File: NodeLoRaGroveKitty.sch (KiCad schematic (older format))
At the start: 43 parts, among them IC1 CP2104, P1 PICKIT PROGRAMMER, P2 Battery, P3 A0, P4 D9, P5 USB_B, P6 I2C, Q1 Q_NPN_CBE, Q2 Q_NPN_CBE, SW2 SW_RESET, U1 AP2114, U2 MCP73831T-2ATI/OT, U3 ESP8266-12E

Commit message: Update BOM
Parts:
- C3: manf# (none) -> GRM21BR61A106KE19L
- IC1: maf# (none) -> CP2104-F03-GM
- P5: manf# (none) -> 105017-0001
- Q1, Q2: value Q_NPN_CBE -> MMBT2222A; manf# (none) -> MMBT2222A
- R16, R17: manf# (none) -> AF0805FR-0710KL
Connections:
- no-connect marks 41 -> 40
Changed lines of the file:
@@
 F 2 "" V 4270 5725 50  0000 C CNN
 F 3 "" V 4270 5725 50  0000 C CNN
+F 4 "105017-0001" H 4320 5825 60  0001 C CNN "manf#"
 	1    4320 5825
 	0    -1   -1   0
@@
 F 7 "USB to UART Bridge" H 5775 6220 50  0001 L CNN "Description"
 F 8 "None" H 5775 6220 50  0001 L CNN "Package"
+F 9 "CP2104-F03-GM" H 5775 6220 60  0001 C CNN "maf#"
 	1    5775 6220
 	1    0    0    -1
@@
 F 2 "" H 4905 6395 50  0000 C CNN
 F 3 "" H 4905 6395 50  0000 C CNN
+F 4 "GRM21BR61A106KE19L" H 4905 6395 60  0001 C CNN "manf#"
 	1    4905 6395
 	1    0    0    -1
@@
 P 5615 3255
 F 0 "Q2" H 5815 3305 50  0000 L CNN
-F 1 "Q_NPN_CBE" H 5815 3205 50  0000 L CNN
+F 1 "MMBT2222A" H 5815 3205 50  0000 L CNN
 F 2 "" H 5815 3355 50  0000 C CNN
 F 3 "" H 5615 3255 50  0000 C CNN
+F 4 "MMBT2222A" H 5615 3255 60  0001 C CNN "manf#"
 	1    5615 3255
 	1    0    0    1
@@
 F 2 "" H 5190 3255 50  0000 C CNN
 F 3 "" H 5190 3255 50  0000 C CNN
+F 4 "AF0805FR-0710KL" H 5190 3255 60  0001 C CNN "manf#"
 	1    5190 3255
 	0    1    1    0
@@
 P 5600 2630
 F 0 "Q1" H 5800 2680 50  0000 L CNN
-F 1 "Q_NPN_CBE" H 5800 2580 50  0000 L CNN
+F 1 "MMBT2222A" H 5800 2580 50  0000 L CNN
 F 2 "" H 5800 2730 50  0000 C CNN
 F 3 "" H 5600 2630 50  0000 C CNN
+F 4 "MMBT2222A" H 5600 2630 60  0001 C CNN "manf#"
 	1    5600 2630
 	1    0    0    -1
@@
 F 2 "" H 5175 2630 50  0000 C CNN
 F 3 "" H 5175 2630 50  0000 C CNN
+F 4 "AF0805FR-0710KL" H 5175 2630 60  0001 C CNN "manf#"
 	1    5175 2630
 	0    1    1    0
@@
 USB TO SERIAL CONVERTER
 NoConn ~ 4220 5525
-NoConn ~ 2215 2965
 $EndSCHEMATC

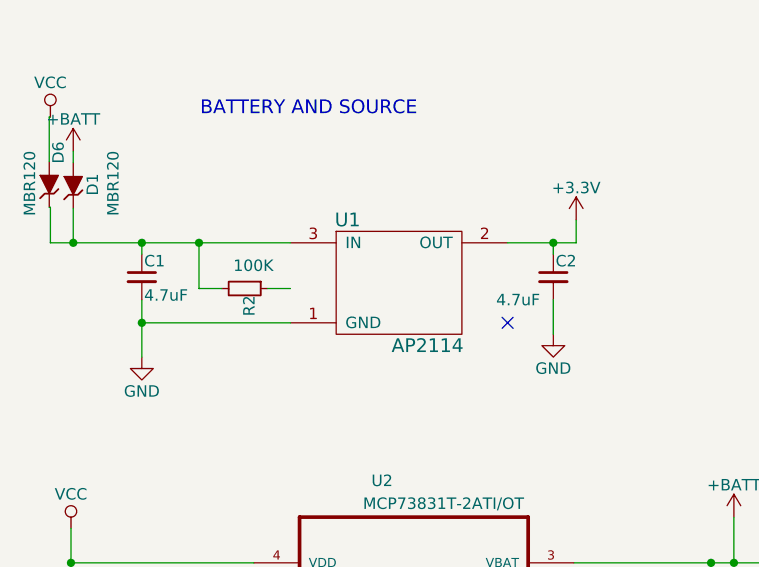
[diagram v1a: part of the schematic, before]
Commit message: Update AP2114, fix bugs JST
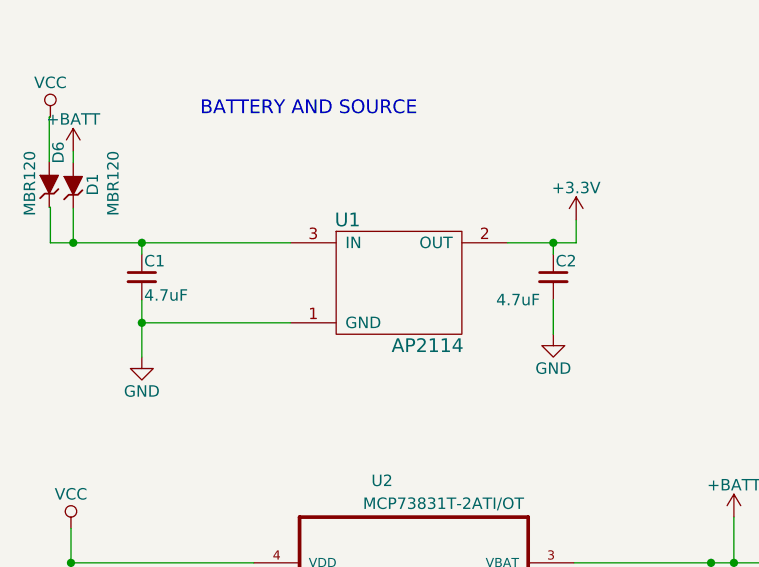
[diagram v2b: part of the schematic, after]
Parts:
- removed R2: 100K, Resistors_SMD:R_0805_HandSoldering, symbol R_Small
- A1: footprint TIH:GSG-SMA-EDGE -> Library:SMA_Conn_Ant
- C3: footprint (none) -> Capacitors_SMD:C_0805_HandSoldering
- D1, D6: footprint Diodes_SMD:SOD-123 -> Diodes_SMD:D_SOD-123
- IC1: footprint QFN24-PAD -> Housings_DFN_QFN:QFN-24_4x4mm_Pitch0.5mm_NoMask
- MODULE1: footprint TIH:RN2483 -> Library:RN2483
- P1: footprint Pin_Headers:Pin_Header_Straight_1x05 -> Pin_Headers:Pin_Header_Straight_1x05_Pitch2.54mm
- P2: footprint Pin_Headers:Pin_Header_Straight_1x02 -> Pin_Headers:Pin_Header_Angled_1x02_Pitch2.54mm
- P3, P4, P6: footprint Connectors_JST:JST_PH_S4B-PH-K_04x2.00mm_Angled -> Connectors_JST:JST_PH_S4B-PH-SM4-TB_04x2.00mm_Angled
- P5: footprint (none) -> LoraCat:MOLEX_105017-0001
- Q1, Q2: footprint (none) -> TO_SOT_Packages_SMD:SOT-23
- R16, R17: footprint (none) -> Resistors_SMD:R_0805_HandSoldering
- SW2: footprint TIH:SW_B3U-1000P -> Buttons_Switches_SMD:SW_SPST_B3U-1000P
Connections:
- no-connect marks 40 -> 39
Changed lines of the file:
@@
 LIBS:contrib
 LIBS:valves
-LIBS:theinventorhouse
 LIBS:USB6B1
 LIBS:MCP73831T-2ATI_OT
-LIBS:antena_good
 LIBS:RN2903-I_RM095
-LIBS:ESP32-footprints-Shem-Lib
 LIBS:CP2104
 LIBS:NodeLoRaGroveKitty-cache
+LIBS:ESP8266
 EELAYER 25 0
 EELAYER END
@@
 F 0 "MODULE1" H 1650 3550 50  0000 L CNN
 F 1 "RN2903" H 1650 750 50  0000 L CNN
-F 2 "TIH:RN2483" H 2250 2150 50  0001 L CNN
+F 2 "Library:RN2483" H 2250 2150 50  0001 L CNN
 F 3 "None" H 2250 2150 50  0001 L CNN
 F 4 "Sub-GHz Dual Band Long Range Transceiver LoRa Module" H 2250 2150 50  0001 L CNN "Description"
@@
 F 0 "P6" H 10950 5500 50  0000 C CNN
 F 1 "I2C" V 11050 5250 50  0000 C CNN
-F 2 "Connectors_JST:JST_PH_S4B-PH-K_04x2.00mm_Angled" H 10950 5250 50  0001 C CNN
+F 2 "Connectors_JST:JST_PH_S4B-PH-SM4-TB_04x2.00mm_Angled" H 10950 5250 50  0001 C CNN
 F 3 "" H 10950 5250 50  0000 C CNN
 F 4 "110990037" H 10950 5250 60  0001 C CNN "manf#"
 	1    10950 5250
 	1    0    0    -1
-$EndComp
-$Comp
-L R_Small R2
-U 1 1 57D1B196
-P 1445 5605
-F 0 "R2" H 1475 5625 50  0000 L CNN
-F 1 "100K" V 1345 5555 50  0000 L CNN
-F 2 "Resistors_SMD:R_0805_HandSoldering" H 1445 5605 50  0001 C CNN
-F 3 "" H 1445 5605 50  0000 C CNN
-F 4 "WR08X1003FTL" H 1445 5605 60  0001 C CNN "manf#"
-	1    1445 5605
-	0    1    1    0
 $EndComp
 $Comp
@@
 F 0 "D1" H 700 5070 50  0000 C CNN
 F 1 "MBR120" H 705 4980 50  0000 C CNN
-F 2 "Diodes_SMD:SOD-123" H 695 5155 50  0001 C CNN
+F 2 "Diodes_SMD:D_SOD-123" H 695 5155 50  0001 C CNN
 F 3 "" H 695 5155 50  0000 C CNN
 F 4 "NRVB120VLSFT1G" H 695 5155 60  0001 C CNN "manf#"
@@
 	0    -1   -1   0
 $EndComp
-NoConn ~ 2595 5755
 $Comp
 L +3.3V #PWR04
@@
 F 0 "P2" H 3935 7005 50  0000 C CNN
 F 1 "Battery" V 4035 6855 50  0000 C CNN
-F 2 "Pin_Headers:Pin_Header_Straight_1x02" H 3935 6855 50  0001 C CNN
+F 2 "Pin_Headers:Pin_Header_Angled_1x02_Pitch2.54mm" H 3935 6855 50  0001 C CNN
 F 3 "" H 3935 6855 50  0000 C CNN
 	1    3935 6855
@@
 F 0 "SW2" H 8630 3770 50  0000 C CNN
 F 1 "SW_RESET" H 8480 3580 50  0000 C CNN
-F 2 "TIH:SW_B3U-1000P" H 8480 3660 50  0001 C CNN
+F 2 "Buttons_Switches_SMD:SW_SPST_B3U-1000P" H 8480 3660 50  0001 C CNN
 F 3 "" H 8480 3660 50  0000 C CNN
 F 4 "B3U-1000P" H 8480 3660 60  0001 C CNN "manf#"
@@
 F 0 "P1" H 3900 3250 50  0000 C CNN
 F 1 "PICKIT PROGRAMMER" V 4000 2950 50  0000 C CNN
-F 2 "Pin_Headers:Pin_Header_Straight_1x05" H 3900 2950 50  0001 C CNN
+F 2 "Pin_Headers:Pin_Header_Straight_1x05_Pitch2.54mm" H 3900 2950 50  0001 C CNN
 F 3 "" H 3900 2950 50  0000 C CNN
 	1    3900 2950
@@
 F 0 "P3" H 9750 5500 50  0000 C CNN
 F 1 "A0" V 9850 5250 50  0000 C CNN
-F 2 "Connectors_JST:JST_PH_S4B-PH-K_04x2.00mm_Angled" H 9750 5250 50  0001 C CNN
+F 2 "Connectors_JST:JST_PH_S4B-PH-SM4-TB_04x2.00mm_Angled" H 9750 5250 50  0001 C CNN
 F 3 "" H 9750 5250 50  0000 C CNN
 F 4 "110990037" H 9750 5250 60  0001 C CNN "manf#"
@@
 F 0 "P4" H 9750 6500 50  0000 C CNN
 F 1 "D9" V 9850 6250 50  0000 C CNN
-F 2 "Connectors_JST:JST_PH_S4B-PH-K_04x2.00mm_Angled" H 9750 6250 50  0001 C CNN
+F 2 "Connectors_JST:JST_PH_S4B-PH-SM4-TB_04x2.00mm_Angled" H 9750 6250 50  0001 C CNN
 F 3 "" H 9750 6250 50  0000 C CNN
 F 4 "110990037" H 9750 6250 60  0001 C CNN "manf#"
@@
 F 0 "A1" H 1600 950 60  0000 C CNN
 F 1 "ANT" H 1600 550 60  0000 C CNN
-F 2 "TIH:GSG-SMA-EDGE" H 1350 550 60  0001 C CNN
+F 2 "Library:SMA_Conn_Ant" H 1350 550 60  0001 C CNN
 F 3 "" H 1350 550 60  0000 C CNN
 	1    1350 550
@@
 F 0 "D6" H 730 5110 50  0000 C CNN
 F 1 "MBR120" H 595 5235 50  0000 C CNN
-F 2 "Diodes_SMD:SOD-123" H 590 5150 50  0001 C CNN
+F 2 "Diodes_SMD:D_SOD-123" H 590 5150 50  0001 C CNN
 F 3 "" H 590 5150 50  0000 C CNN
 F 4 "NRVB120VLSFT1G" H 590 5150 60  0001 C CNN "manf#"
@@
 F 0 "P5" H 4520 5625 50  0000 C CNN
 F 1 "USB_B" H 4270 6025 50  0000 C CNN
-F 2 "" V 4270 5725 50  0000 C CNN
+F 2 "LoraCat:MOLEX_105017-0001" V 4270 5725 50  0001 C CNN
 F 3 "" V 4270 5725 50  0000 C CNN
 F 4 "105017-0001" H 4320 5825 60  0001 C CNN "manf#"
@@
 F 0 "IC1" H 5275 7220 50  0000 L CNN
 F 1 "CP2104" H 5275 5220 50  0000 L CNN
-F 2 "QFN24-PAD" H 5775 6220 50  0001 L CNN
+F 2 "Housings_DFN_QFN:QFN-24_4x4mm_Pitch0.5mm_NoMask" H 5775 6220 50  0001 L CNN
 F 3 "None" H 5775 6220 50  0001 L CNN
 F 4 "Silicon Labs" H 5775 6220 50  0001 L CNN "MF"
@@
 F 0 "C3" H 4915 6465 50  0000 L CNN
 F 1 "10uF" H 4580 6330 50  0000 L CNN
-F 2 "" H 4905 6395 50  0000 C CNN
+F 2 "Capacitors_SMD:C_0805_HandSoldering" H 4905 6395 50  0001 C CNN
 F 3 "" H 4905 6395 50  0000 C CNN
 F 4 "GRM21BR61A106KE19L" H 4905 6395 60  0001 C CNN "manf#"
@@
 F 0 "Q2" H 5815 3305 50  0000 L CNN
 F 1 "MMBT2222A" H 5815 3205 50  0000 L CNN
-F 2 "" H 5815 3355 50  0000 C CNN
+F 2 "TO_SOT_Packages_SMD:SOT-23" H 5815 3355 50  0001 C CNN
 F 3 "" H 5615 3255 50  0000 C CNN
 F 4 "MMBT2222A" H 5615 3255 60  0001 C CNN "manf#"
@@
 F 0 "R17" H 5220 3275 50  0000 L CNN
 F 1 "10K" H 5220 3215 50  0000 L CNN
-F 2 "" H 5190 3255 50  0000 C CNN
+F 2 "Resistors_SMD:R_0805_HandSoldering" H 5190 3255 50  0001 C CNN
 F 3 "" H 5190 3255 50  0000 C CNN
 F 4 "AF0805FR-0710KL" H 5190 3255 60  0001 C CNN "manf#"
@@
 F 0 "Q1" H 5800 2680 50  0000 L CNN
 F 1 "MMBT2222A" H 5800 2580 50  0000 L CNN
-F 2 "" H 5800 2730 50  0000 C CNN
+F 2 "TO_SOT_Packages_SMD:SOT-23" H 5800 2730 50  0001 C CNN
 F 3 "" H 5600 2630 50  0000 C CNN
 F 4 "MMBT2222A" H 5600 2630 60  0001 C CNN "manf#"
@@
 F 0 "R16" H 5205 2650 50  0000 L CNN
 F 1 "10K" H 5205 2590 50  0000 L CNN
-F 2 "" H 5175 2630 50  0000 C CNN
+F 2 "Resistors_SMD:R_0805_HandSoldering" H 5175 2630 50  0001 C CNN
 F 3 "" H 5175 2630 50  0000 C CNN
 F 4 "AF0805FR-0710KL" H 5175 2630 60  0001 C CNN "manf#"
@@
 Wire Wire Line
 	995  5405 995  5455
-Connection ~ 1245 5405
-Wire Wire Line
-	1245 5405 1245 5605
-Wire Wire Line
-	1245 5605 1345 5605
-Wire Wire Line
-	1545 5605 1645 5605
 Wire Wire Line
 	695  5255 695  5405

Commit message: New design PCB
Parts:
- P4: renamed from P3; footprint Connectors_JST:JST_PH_S4B-PH-SM4-TB_04x2.00mm_Angled -> Library:JST_PH_S4B-PH-SM4-TB_04x2.00mm_Angled
- P5: renamed from P4; footprint Connectors_JST:JST_PH_S4B-PH-SM4-TB_04x2.00mm_Angled -> Library:JST_PH_S4B-PH-SM4-TB_04x2.00mm_Angled
- P6: footprint Connectors_JST:JST_PH_S4B-PH-SM4-TB_04x2.00mm_Angled -> Library:JST_PH_S4B-PH-SM4-TB_04x2.00mm_Angled
- U1: footprint TO_SOT_Packages_SMD:SOT-223 -> TO_SOT_Packages_SMD:SOT-223-3Lead_TabPin2
- renumbered C4 to C3, C6 to C4, C3 to C6, D6 to D1, D1 to D2, D2 to D5, P5 to P3, R4 to R1, R1 to R10, R12 to R11, R13 to R12, R9 to R13, R6 to R14, R7 to R15, R15 to R16, R5 to R2, R11 to R3, R3 to R4, R8 to R5, R16 to R6, R17 to R7, R10 to R8, R14 to R9, SW2 to SW1
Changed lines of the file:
@@
 F 0 "U1" H 1895 5905 60  0000 C CNN
 F 1 "AP2114" H 2245 5355 60  0000 C CNN
-F 2 "TO_SOT_Packages_SMD:SOT-223" H 2095 5605 60  0001 C CNN
+F 2 "TO_SOT_Packages_SMD:SOT-223-3Lead_TabPin2" H 2095 5605 60  0001 C CNN
 F 3 "" H 2095 5605 60  0000 C CNN
 F 4 "AP2114H-3.3TRG1" H 2095 5605 60  0001 C CNN "manf#"
@@
 F 0 "P6" H 10950 5500 50  0000 C CNN
 F 1 "I2C" V 11050 5250 50  0000 C CNN
-F 2 "Connectors_JST:JST_PH_S4B-PH-SM4-TB_04x2.00mm_Angled" H 10950 5250 50  0001 C CNN
+F 2 "Library:JST_PH_S4B-PH-SM4-TB_04x2.00mm_Angled" H 10950 5250 50  0001 C CNN
 F 3 "" H 10950 5250 50  0000 C CNN
 F 4 "110990037" H 10950 5250 60  0001 C CNN "manf#"
@@
 $EndComp
 $Comp
-L ZENERsmall D1
+L ZENERsmall D2
 U 1 1 57D1B9F5
 P 695 5155
-F 0 "D1" H 700 5070 50  0000 C CNN
+F 0 "D2" H 700 5070 50  0000 C CNN
 F 1 "MBR120" H 705 4980 50  0000 C CNN
 F 2 "Diodes_SMD:D_SOD-123" H 695 5155 50  0001 C CNN
@@
 $EndComp
 $Comp
-L R_Small R11
+L R_Small R3
 U 1 1 57D1C984
 P 3285 7105
-F 0 "R11" H 3315 7125 50  0000 L CNN
+F 0 "R3" H 3315 7125 50  0000 L CNN
 F 1 "10K" H 3315 7065 50  0000 L CNN
 F 2 "Resistors_SMD:R_0805_HandSoldering" H 3285 7105 50  0001 C CNN
@@
 $EndComp
 $Comp
-L R_Small R4
+L R_Small R1
 U 1 1 57D1D2C1
 P 1235 7005
-F 0 "R4" H 1265 7025 50  0000 L CNN
+F 0 "R1" H 1265 7025 50  0000 L CNN
 F 1 "330R" H 1265 6965 50  0000 L CNN
 F 2 "Resistors_SMD:R_0805_HandSoldering" H 1235 7005 50  0001 C CNN
@@
 $EndComp
 $Comp
-L R_Small R5
+L R_Small R2
 U 1 1 57D1DE4B
 P 1235 7305
-F 0 "R5" H 1265 7325 50  0000 L CNN
+F 0 "R2" H 1265 7325 50  0000 L CNN
 F 1 "330R" H 1265 7265 50  0000 L CNN
 F 2 "Resistors_SMD:R_0805_HandSoldering" H 1235 7305 50  0001 C CNN
@@
 $EndComp
 $Comp
-L C_Small C6
+L C_Small C4
 U 1 1 57D1EF29
 P 3485 7055
-F 0 "C6" H 3495 7125 50  0000 L CNN
+F 0 "C4" H 3495 7125 50  0000 L CNN
 F 1 "10uF" H 3495 6975 50  0000 L CNN
 F 2 "Capacitors_SMD:C_0805_HandSoldering" H 3485 7055 50  0001 C CNN
@@
 $EndComp
 $Comp
-L R_Small R13
+L R_Small R12
 U 1 1 57D1F4A1
 P 8450 5600
-F 0 "R13" H 8480 5620 50  0000 L CNN
+F 0 "R12" H 8480 5620 50  0000 L CNN
 F 1 "4.7K" H 8480 5560 50  0000 L CNN
 F 2 "Resistors_SMD:R_0805_HandSoldering" H 8450 5600 50  0001 C CNN
@@
 $EndComp
 $Comp
-L R_Small R12
+L R_Small R11
 U 1 1 57D1F516
 P 8200 5600
-F 0 "R12" H 8230 5620 50  0000 L CNN
+F 0 "R11" H 8230 5620 50  0000 L CNN
 F 1 "4.7K" H 8230 5560 50  0000 L CNN
 F 2 "Resistors_SMD:R_0805_HandSoldering" H 8200 5600 50  0001 C CNN
@@
 SCL
 $Comp
-L SW_PUSH SW2
+L SW_PUSH SW1
 U 1 1 57D1FEE4
 P 8480 3660
-F 0 "SW2" H 8630 3770 50  0000 C CNN
+F 0 "SW1" H 8630 3770 50  0000 C CNN
 F 1 "SW_RESET" H 8480 3580 50  0000 C CNN
 F 2 "Buttons_Switches_SMD:SW_SPST_B3U-1000P" H 8480 3660 50  0001 C CNN
@@
 $EndComp
 $Comp
-L R_Small R9
+L R_Small R13
 U 1 1 57D20283
 P 8930 3410
-F 0 "R9" H 8960 3430 50  0000 L CNN
+F 0 "R13" H 8960 3430 50  0000 L CNN
 F 1 "10K" H 8960 3370 50  0000 L CNN
 F 2 "Resistors_SMD:R_0805_HandSoldering" H 8930 3410 50  0001 C CNN
@@
 RST_RN
 $Comp
-L R_Small R3
+L R_Small R4
 U 1 1 57D21637
 P 3650 2550
-F 0 "R3" H 3680 2570 50  0000 L CNN
+F 0 "R4" H 3680 2570 50  0000 L CNN
 F 1 "10K" H 3680 2510 50  0000 L CNN
 F 2 "Resistors_SMD:R_0805_HandSoldering" H 3650 2550 50  0001 C CNN
@@
 $EndComp
 $Comp
-L CONN_01X04 P3
+L CONN_01X04 P4
 U 1 1 57D23072
 P 9750 5250
-F 0 "P3" H 9750 5500 50  0000 C CNN
+F 0 "P4" H 9750 5500 50  0000 C CNN
 F 1 "A0" V 9850 5250 50  0000 C CNN
-F 2 "Connectors_JST:JST_PH_S4B-PH-SM4-TB_04x2.00mm_Angled" H 9750 5250 50  0001 C CNN
+F 2 "Library:JST_PH_S4B-PH-SM4-TB_04x2.00mm_Angled" H 9750 5250 50  0001 C CNN
 F 3 "" H 9750 5250 50  0000 C CNN
 F 4 "110990037" H 9750 5250 60  0001 C CNN "manf#"
@@
 $EndComp
 $Comp
-L CONN_01X04 P4
+L CONN_01X04 P5
 U 1 1 57D230DD
 P 9750 6250
-F 0 "P4" H 9750 6500 50  0000 C CNN
+F 0 "P5" H 9750 6500 50  0000 C CNN
 F 1 "D9" V 9850 6250 50  0000 C CNN
-F 2 "Connectors_JST:JST_PH_S4B-PH-SM4-TB_04x2.00mm_Angled" H 9750 6250 50  0001 C CNN
+F 2 "Library:JST_PH_S4B-PH-SM4-TB_04x2.00mm_Angled" H 9750 6250 50  0001 C CNN
 F 3 "" H 9750 6250 50  0000 C CNN
 F 4 "110990037" H 9750 6250 60  0001 C CNN "manf#"
@@
 $EndComp
 $Comp
-L C_Small C4
+L C_Small C3
 U 1 1 57D23565
 P 3450 1050
-F 0 "C4" H 3460 1120 50  0000 L CNN
+F 0 "C3" H 3460 1120 50  0000 L CNN
 F 1 "0.1uF" H 3460 970 50  0000 L CNN
 F 2 "Capacitors_SMD:C_0805_HandSoldering" H 3450 1050 50  0001 C CNN
@@
 NoConn ~ 1450 1950
 $Comp
-L R R6
+L R R14
 U 1 1 58091A86
 P 10275 3840
-F 0 "R6" V 10355 3840 50  0000 C CNN
+F 0 "R14" V 10355 3840 50  0000 C CNN
 F 1 "10K" V 10275 3840 50  0000 C CNN
 F 2 "Resistors_SMD:R_0805_HandSoldering" V 10205 3840 50  0001 C CNN
@@
 GPIO15
 $Comp
-L R R7
+L R R15
 U 1 1 58092BBE
 P 10575 3990
-F 0 "R7" V 10655 3990 50  0000 C CNN
+F 0 "R15" V 10655 3990 50  0000 C CNN
 F 1 "10K" V 10575 3990 50  0000 C CNN
 F 2 "Resistors_SMD:R_0805_HandSoldering" V 10505 3990 50  0001 C CNN
@@
 $EndComp
 $Comp
-L R R8
+L R R5
 U 1 1 58097BD5
 P 4925 1055
-F 0 "R8" V 5005 1055 50  0000 C CNN
+F 0 "R5" V 5005 1055 50  0000 C CNN
 F 1 "100K" V 4925 1055 50  0000 C CNN
 F 2 "Resistors_SMD:R_0805_HandSoldering" V 4855 1055 50  0001 C CNN
@@
 $EndComp
 $Comp
-L R R10
+L R R8
 U 1 1 58097C60
 P 5345 1055
-F 0 "R10" V 5425 1055 50  0000 C CNN
+F 0 "R8" V 5425 1055 50  0000 C CNN
 F 1 "100K" V 5345 1055 50  0000 C CNN
 F 2 "Resistors_SMD:R_0805_HandSoldering" V 5275 1055 50  0001 C CNN
@@
 Voltage Divider of 3.3v to 1.1v
 $Comp
-L R R14
+L R R9
 U 1 1 585145DF
 P 5905 1055
-F 0 "R14" V 5985 1055 50  0000 C CNN
+F 0 "R9" V 5985 1055 50  0000 C CNN
 F 1 "100K" V 5905 1055 50  0000 C CNN
 F 2 "Resistors_SMD:R_0805_HandSoldering" V 5835 1055 50  0001 C CNN
@@
 $EndComp
 $Comp
-L R R15
+L R R16
 U 1 1 58543F5A
 P 10900 3870
-F 0 "R15" V 10980 3870 50  0000 C CNN
+F 0 "R16" V 10980 3870 50  0000 C CNN
 F 1 "10K" V 10900 3870 50  0000 C CNN
 F 2 "Resistors_SMD:R_0805_HandSoldering" V 10830 3870 50  0001 C CNN
@@
 $EndComp
 $Comp
-L ZENERsmall D6
+L ZENERsmall D1
 U 1 1 58924335
 P 590 5150
-F 0 "D6" H 730 5110 50  0000 C CNN
+F 0 "D1" H 730 5110 50  0000 C CNN
 F 1 "MBR120" H 595 5235 50  0000 C CNN
 F 2 "Diodes_SMD:D_SOD-123" H 590 5150 50  0001 C CNN
@@
 $EndComp
 $Comp
-L Led_Small D2
+L Led_Small D5
 U 1 1 57D23DF7
 P 7495 3895
-F 0 "D2" H 7445 4020 50  0000 L CNN
+F 0 "D5" H 7445 4020 50  0000 L CNN
 F 1 "Led" H 7345 3845 50  0000 L CNN
 F 2 "LEDs:LED_0805" V 7495 3895 50  0001 C CNN
@@
 $EndComp
 $Comp
-L R_Small R1
+L R_Small R10
 U 1 1 57D2387F
 P 7495 3595
-F 0 "R1" H 7525 3615 50  0000 L CNN
+F 0 "R10" H 7525 3615 50  0000 L CNN
 F 1 "330R" H 7495 3495 50  0000 L CNN
 F 2 "Resistors_SMD:R_0805_HandSoldering" H 7495 3595 50  0001 C CNN
@@
 GPIO0
 $Comp
-L USB_B P5
+L USB_B P3
 U 1 1 58A60EE9
 P 4320 5825
-F 0 "P5" H 4520 5625 50  0000 C CNN
+F 0 "P3" H 4520 5625 50  0000 C CNN
 F 1 "USB_B" H 4270 6025 50  0000 C CNN
 F 2 "LoraCat:MOLEX_105017-0001" V 4270 5725 50  0001 C CNN
@@
 $EndComp
 $Comp
-L C_Small C3
+L C_Small C6
 U 1 1 58A664F1
 P 4905 6395
-F 0 "C3" H 4915 6465 50  0000 L CNN
+F 0 "C6" H 4915 6465 50  0000 L CNN
 F 1 "10uF" H 4580 6330 50  0000 L CNN
 F 2 "Capacitors_SMD:C_0805_HandSoldering" H 4905 6395 50  0001 C CNN
@@
 $EndComp
 $Comp
-L R_Small R17
+L R_Small R7
 U 1 1 58A6DCAB
 P 5190 3255
-F 0 "R17" H 5220 3275 50  0000 L CNN
+F 0 "R7" H 5220 3275 50  0000 L CNN
 F 1 "10K" H 5220 3215 50  0000 L CNN
 F 2 "Resistors_SMD:R_0805_HandSoldering" H 5190 3255 50  0001 C CNN
@@
 $EndComp
 $Comp
-L R_Small R16
+L R_Small R6
 U 1 1 58A6E586
 P 5175 2630
-F 0 "R16" H 5205 2650 50  0000 L CNN
+F 0 "R6" H 5205 2650 50  0000 L CNN
 F 1 "10K" H 5205 2590 50  0000 L CNN
 F 2 "Resistors_SMD:R_0805_HandSoldering" H 5175 2630 50  0001 C CNN

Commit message: PCB 1.0v
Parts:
- P2: footprint Pin_Headers:Pin_Header_Angled_1x02_Pitch2.54mm -> modules:panelmate_smd_2
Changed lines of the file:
@@
 F 0 "P2" H 3935 7005 50  0000 C CNN
 F 1 "Battery" V 4035 6855 50  0000 C CNN
-F 2 "Pin_Headers:Pin_Header_Angled_1x02_Pitch2.54mm" H 3935 6855 50  0001 C CNN
+F 2 "modules:panelmate_smd_2" H 3935 6855 50  0001 C CNN
 F 3 "" H 3935 6855 50  0000 C CNN
 	1    3935 6855

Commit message: Update BOM
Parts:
- A1: manf# (none) -> CONREVSMA003.031
- IC1: maf# CP2104-F03-GM -> (none); manf# (none) -> CP2104-F03-GM
- P4, P5, P6: manf# 110990037 -> 110990030
- U1: symbol AP2112 -> AP2112-RESCUE-NodeLoRaGroveKitty
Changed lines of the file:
@@
 EESchema Schematic File Version 2
+LIBS:NodeLoRaGroveKitty-rescue
 LIBS:power
 LIBS:device
@@
 LIBS:contrib
 LIBS:valves
+LIBS:theinventorhouse
 LIBS:USB6B1
 LIBS:MCP73831T-2ATI_OT
+LIBS:antena_good
 LIBS:RN2903-I_RM095
+LIBS:ESP32-footprints-Shem-Lib
 LIBS:CP2104
 LIBS:NodeLoRaGroveKitty-cache
-LIBS:ESP8266
 EELAYER 25 0
 EELAYER END
@@
 $EndComp
 $Comp
-L AP2112 U1
+L AP2112-RESCUE-NodeLoRaGroveKitty U1
 U 1 1 57D06EC7
 P 2095 5605
@@
 F 2 "Library:JST_PH_S4B-PH-SM4-TB_04x2.00mm_Angled" H 10950 5250 50  0001 C CNN
 F 3 "" H 10950 5250 50  0000 C CNN
-F 4 "110990037" H 10950 5250 60  0001 C CNN "manf#"
+F 4 "110990030" H 10950 5250 60  0001 C CNN "manf#"
 	1    10950 5250
 	1    0    0    -1
@@
 F 2 "Library:JST_PH_S4B-PH-SM4-TB_04x2.00mm_Angled" H 9750 5250 50  0001 C CNN
 F 3 "" H 9750 5250 50  0000 C CNN
-F 4 "110990037" H 9750 5250 60  0001 C CNN "manf#"
+F 4 "110990030" H 9750 5250 60  0001 C CNN "manf#"
 	1    9750 5250
 	1    0    0    -1
@@
 F 2 "Library:JST_PH_S4B-PH-SM4-TB_04x2.00mm_Angled" H 9750 6250 50  0001 C CNN
 F 3 "" H 9750 6250 50  0000 C CNN
-F 4 "110990037" H 9750 6250 60  0001 C CNN "manf#"
+F 4 "110990030" H 9750 6250 60  0001 C CNN "manf#"
 	1    9750 6250
 	1    0    0    -1
@@
 F 2 "Library:SMA_Conn_Ant" H 1350 550 60  0001 C CNN
 F 3 "" H 1350 550 60  0000 C CNN
+F 4 "CONREVSMA003.031" H 1350 550 60  0001 C CNN "manf#"
 	1    1350 550
 	-1   0    0    1
@@
 F 7 "USB to UART Bridge" H 5775 6220 50  0001 L CNN "Description"
 F 8 "None" H 5775 6220 50  0001 L CNN "Package"
-F 9 "CP2104-F03-GM" H 5775 6220 60  0001 C CNN "maf#"
+F 9 "CP2104-F03-GM" H 5775 6220 60  0001 C CNN "manf#"
 	1    5775 6220
 	1    0    0    -1
